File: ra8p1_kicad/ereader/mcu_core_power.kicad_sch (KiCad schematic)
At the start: 17 parts, among them U1 R7KA8P1KFLCAC#UC0

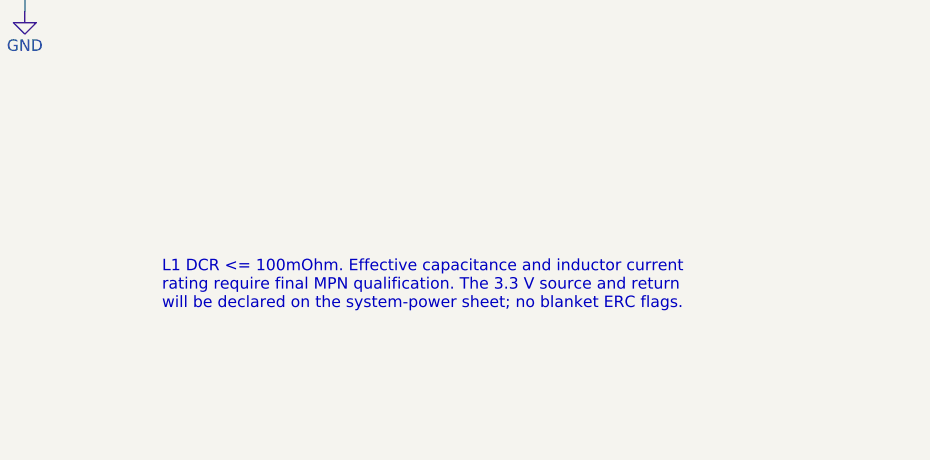
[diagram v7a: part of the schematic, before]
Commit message: Implement main digital supply with linked engineering calculations
Wire the TPS63802 converter and its hierarchical enable, source its exact BOM, and refresh the full nine-page schematic PDF. Preserve the SDRAM pin and timing contract for the memory implementation. Track #825 and #827; system qualification remains open.
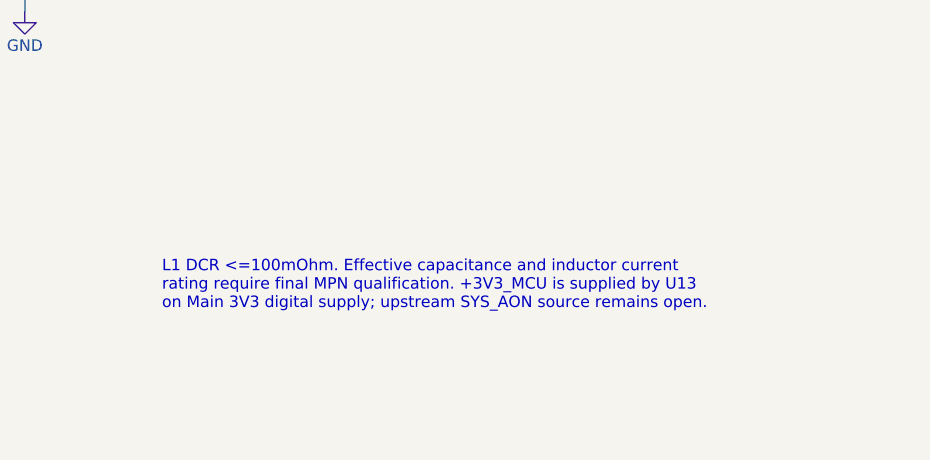
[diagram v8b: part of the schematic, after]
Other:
- note added: "L1 DCR <=100mOhm. Effective capacitance and inductor current rating require final MPN qualification. +3V3_MCU is supplied by U13 on Main 3V3 digital supply; upstream SYS_AON source remains open."
- note removed: "L1 DCR <= 100mOhm. Effective capacitance and inductor current rating require final MPN qualification. The 3.3 V source and return will be declared on the system-power sheet; no blanket ERC flags."
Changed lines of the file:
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@@
 		)
 	)
-	(text "L1 DCR <= 100mOhm. Effective capacitance and inductor current\nrating require final MPN qualification. The 3.3 V source and return\nwill be declared on the system-power sheet; no blanket ERC flags."
+	(text "L1 DCR <=100mOhm. Effective capacitance and inductor current\nrating require final MPN qualification. +3V3_MCU is supplied by U13\non Main 3V3 digital supply; upstream SYS_AON source remains open."
 		(exclude_from_sim no)
 		(at 269.24 220.98 0)
